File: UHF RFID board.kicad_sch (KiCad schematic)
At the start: 29 parts, among them J1 FZ_full_module, J2 picoblade, J4 ICSP, J5 SPI, U1 YRM1001, U2 SEC1210

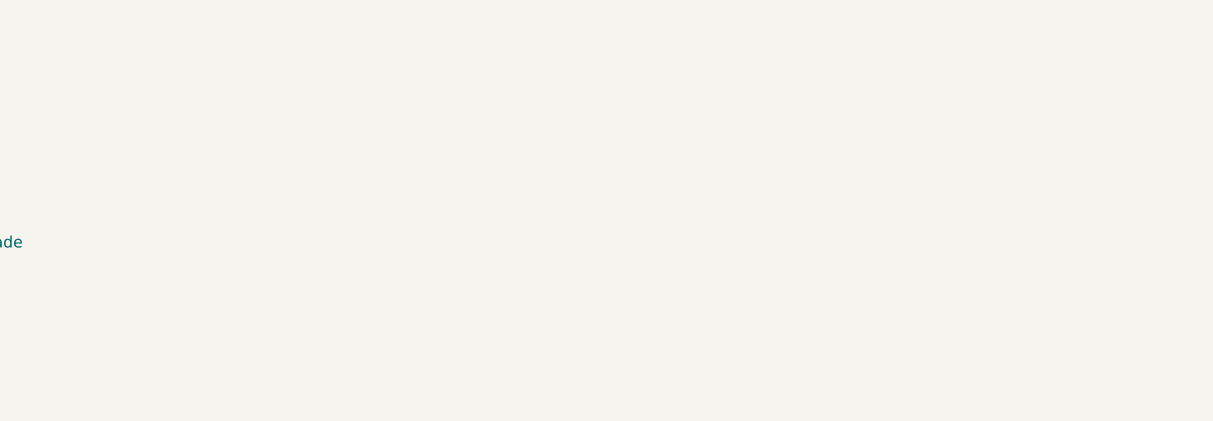
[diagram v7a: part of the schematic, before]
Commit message: futureproofing for automated production
Added fiducial markers for automated PNP machine assembly capability.
updated version from 2.4 to 2.5
added version info in schematic, along with title and my name for credit
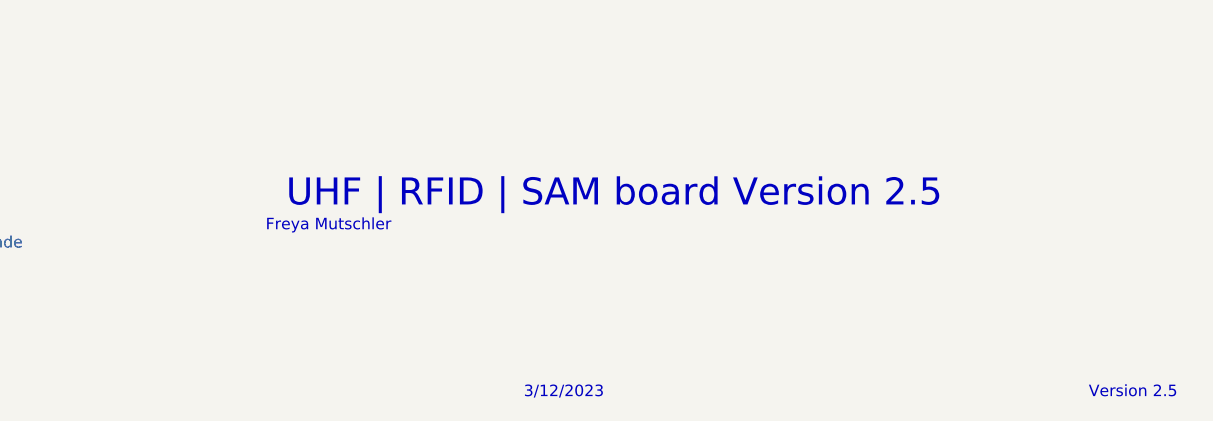
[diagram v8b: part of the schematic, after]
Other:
- note added: "3/12/2023"
- note added: "Freya Mutschler"
- note added: "UHF | RFID | SAM board Version 2.5"
- note added: "Version 2.5"
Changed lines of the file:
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@@
+		)
+	)
+	(text "3/12/2023"
+		(exclude_from_sim no)
+		(at 212.09 193.294 0)
+		(effects
+			(font
+				(size 1.27 1.27)
+			)
+		)
+	)
+	(text "Version 2.5"
+		(exclude_from_sim no)
+		(at 275.336 193.294 0)
+		(effects
+			(font
+				(size 1.27 1.27)
+			)
+		)
+	)
+	(text "Freya Mutschler"
+		(exclude_from_sim no)
+		(at 185.928 174.752 0)
+		(effects
+			(font
+				(size 1.27 1.27)
+			)
+		)
+	)
+	(text "UHF | RFID | SAM board Version 2.5"
+		(exclude_from_sim no)
+		(at 217.678 171.196 0)
+		(effects
+			(font
+				(face "Verdana")
+				(size 3 3)
+			)
 		)
 	)
